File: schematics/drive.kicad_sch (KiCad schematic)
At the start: 24 parts, among them J1 EncoderConn, J2 EncoderConn, J3 EncoderConn, U1 MP6550GG-Z, U2 MP6550GG-Z, U3 MP6550GG-Z

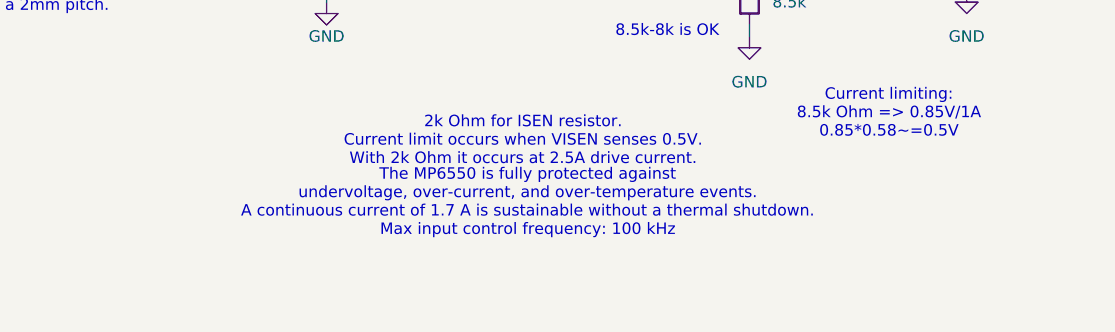
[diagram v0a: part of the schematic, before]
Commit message: Fixed mistake in battery bypass circuit.
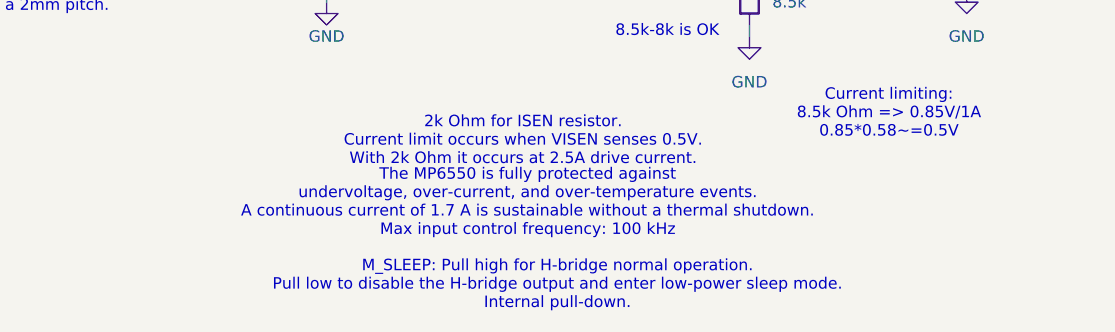
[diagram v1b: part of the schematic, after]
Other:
- note added: "M_SLEEP: Pull high for H-bridge normal operation. Pull low to disable the H-bridge output and enter low-power sleep mode. Internal pull-down."
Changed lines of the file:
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@@
+		)
+	)
+	(text "M_SLEEP: Pull high for H-bridge normal operation. \nPull low to disable the H-bridge output and enter low-power sleep mode. \nInternal pull-down."
+		(exclude_from_sim no)
+		(at 127.254 158.496 0)
+		(effects
+			(font
+				(size 1.27 1.27)
+			)
 		)
 	)
